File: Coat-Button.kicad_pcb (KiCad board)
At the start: 2 copper layers, 18 x 18 mm, 22 parts, among them P1 CONN_1, P2 CONN_1, P3 CONN_1, P4 CONN_1

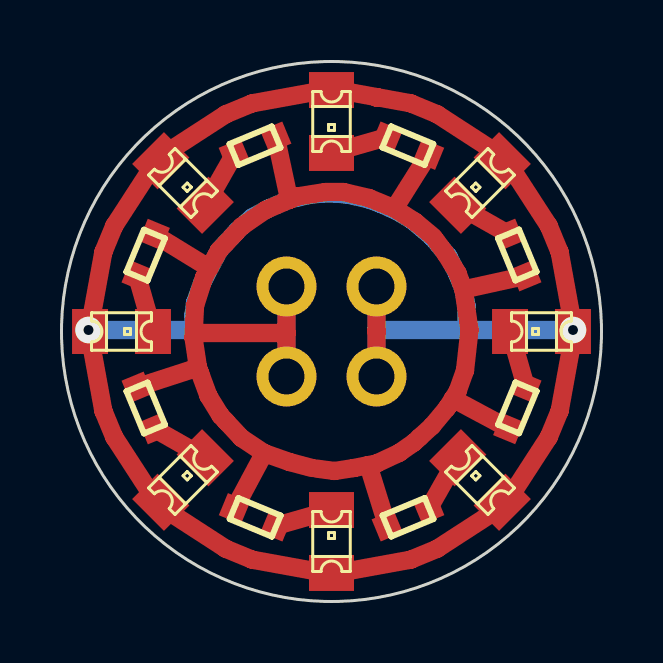
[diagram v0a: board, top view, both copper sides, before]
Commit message: Managed to get an ATtiny13 (DFN10) on there again ;-)
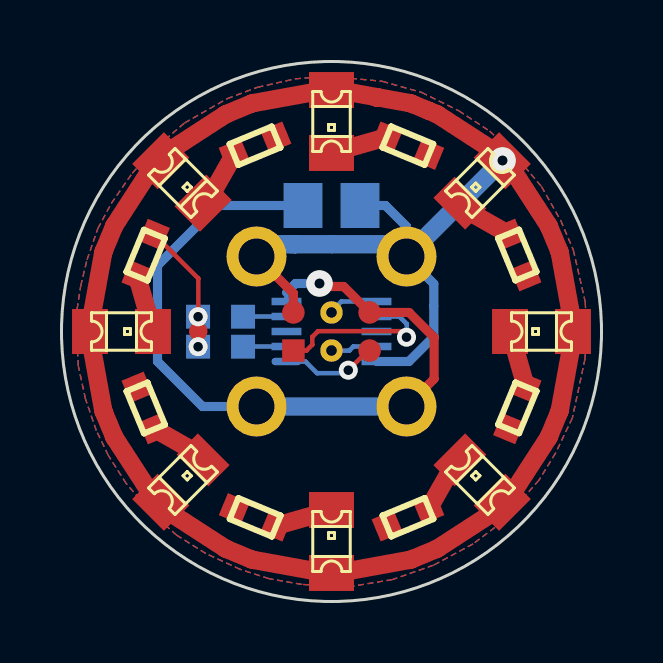
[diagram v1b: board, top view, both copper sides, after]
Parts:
- removed the G*** at (75.0, 56.4)
- removed the G*** at (75.0, 68.1)
- added C1: 4.7µF, MADW__C0805, B.Cu at (75.0, 57.8)
- added G***: OSHW-logo_silkscreen_3mm, OSHW-logo_silkscreen_3mm, B.Cu at (68.0, 62.0)
- added G***: LED_smile_silkscreen_3mm, LED_smile_silkscreen_3mm, B.Cu at (81.5, 62.0)
- added IC1: MADW__ATTINY13-MM, MADW__MLF10, B.Cu at (75.0, 62.0)
- added JP1: AVR_ISP, MADW__PIN_ARRAY_3x2_1.27mm, F.Cu at (75.0, 62.0)
- added R10: 15, MADW__R0603, B.Cu at (71.3, 61.5)
- added R9: 15, MADW__R0603, B.Cu at (71.3, 62.5)
- moved P1 1.41 mm to (72.5, 59.5)
- moved P2 1.41 mm to (77.5, 59.5)
- moved P3 1.41 mm to (72.5, 64.5)
- moved P4 1.41 mm to (77.5, 64.5)
- renumbered P3 to P1, P4 to P3, P1 to P4
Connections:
- P1 pad 1: GND -> VCC
- P4 pad 1: VCC -> GND
- R1 pad 1: GND -> /sink
- R2 pad 1: GND -> /sink
- R3 pad 1: GND -> /sink
- R4 pad 1: GND -> /sink
- R5 pad 1: GND -> /sink
- R6 pad 1: GND -> /sink
- R7 pad 1: GND -> /sink
- R8 pad 1: GND -> /sink
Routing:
- net GND: track 55.2 -> 26.6 mm, vias 0 -> 1
- net VCC: track 81.0 -> 71.2 mm, vias 2 -> 1
- net MISO: track 0.00 -> 5.83 mm, vias 0 -> 1
- net /sink: track 0.00 -> 4.92 mm, vias 0 -> 2
- net RST: track 0.00 -> 3.24 mm, vias 0 -> 1
- net MOSI: track 0.00 -> 1.67 mm
- net SCK: track 0.00 -> 1.56 mm
- net N-0000011: track 0.00 -> 1.45 mm
- net N-0000010: track 0.00 -> 1.45 mm
- added copper zone on F.Cu, net /sink
- added copper zone on B.Cu, net GND
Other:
- board text added: "2013 V0.11.a"
- board text removed: "2013"

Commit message: Tweaks. Added solder-bridge if no micro is used.
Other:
- board text added: "2013 V0.11.b"
- board text added: "MCU?"
- board text removed: "2013 V0.11.a"
